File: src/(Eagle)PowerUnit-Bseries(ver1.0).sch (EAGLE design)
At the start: 51 parts

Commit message: XT60PWコネクタに変えた
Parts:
- removed IN+, IN-, OUT1+, OUT1-, OUT2+, OUT2-, OUT3+, OUT3-, THRU+, THRU-: PADS14, OKUDA_libraries:PADS14
- added CON1: XT90PW-M, amass:XT90PW-M
- added CON2: XT90PW-F, amass:XT90PW-F
- added CON3, CON4, CON5, CON6: XT60PW-F, amass:XT60PW-F
- added U1: LQFP64, STM32F446xC:LQFP64
- added U2: MCP2517FD, MCP2517FD:MCP2517FD
- H1, H2, H3, H4: value MOUNT-HOLE3.2 -> MOUNT-HOLE3.2(NORESIST); device holes:MOUNT-HOLE3.2 -> MOUNT-HOLE3.2(NORESIST):MOUNT-HOLE3.2(NORESIST)
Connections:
- net GND: now also CON1.-, CON2.-, H1.P$1, H2.P$1, H3.P$1, H4.P$1; no longer IN-.P$1, THRU-.P$1
- net N$1: now also CON3.-; no longer OUT1-.P$1
- net N$2: now also CON4.-; no longer OUT2-.P$1
- net N$4: now also CON3.+; no longer OUT1+.P$1
- net N$5: now also CON4.+; no longer OUT2+.P$1
- net N$6: no longer OUT3+.P$1
- net N$9: no longer OUT3-.P$1
- net VCC: now also CON1.+, CON2.+; no longer IN+.P$1, THRU+.P$1
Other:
- note removed: "e2011220_竹内一晴"
- note removed: "新電源基板(仮)_回路図"
- note removed: "部品選定完了☑"

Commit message: トランシーバ選定途中、XT60PW
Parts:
- removed EDGE5: 7-5530843-6, 7-5530843-6:7-5530843-6
- removed OUT4+, OUT4-: PADS14, OKUDA_libraries:PADS14
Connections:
- removed net NC: EDGE5.P7
- net DIR1: no longer EDGE5.P12
- net DIR2: no longer EDGE5.P11
- net DIR3: no longer EDGE5.P10
- net DIR4: no longer EDGE5.P9
- net GND2: no longer EDGE5.P8
- net LED: no longer EDGE5.P6
- net N$10: now also CON6.+; no longer OUT4+.P$1
- net N$13: now also CON6.-; no longer OUT4-.P$1
- net N$6: now also CON5.+
- net N$9: now also CON5.-
- net PWM1: no longer EDGE5.P1
- net PWM2: no longer EDGE5.P2
- net PWM3: no longer EDGE5.P3
- net PWM4: no longer EDGE5.P4
- net VCC2: no longer EDGE5.P5
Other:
- note removed: "MDC input"
- moved on the sheet: CON6, LED2, R1

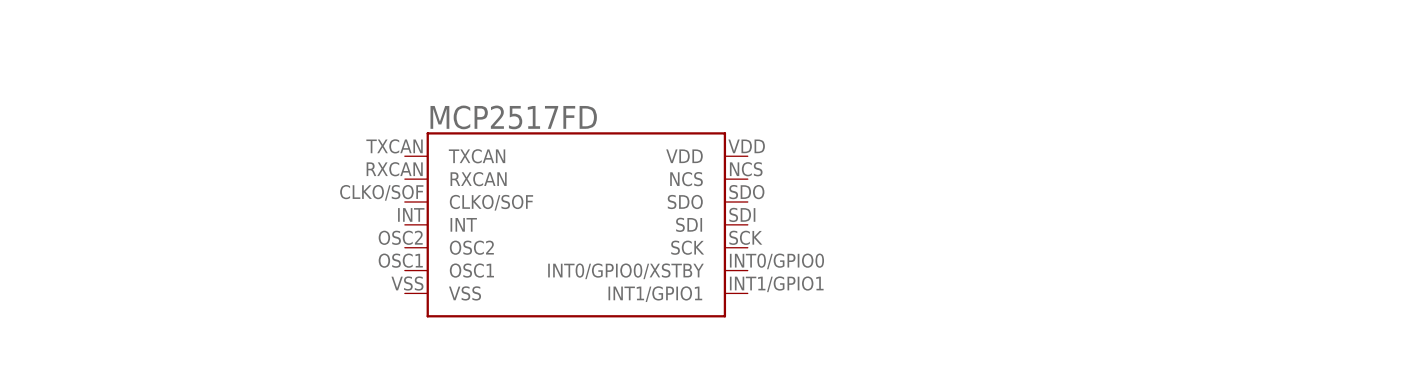
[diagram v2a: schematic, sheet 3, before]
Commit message: CANトランシーバの選定(クリスマスイブですよ？（笑）)
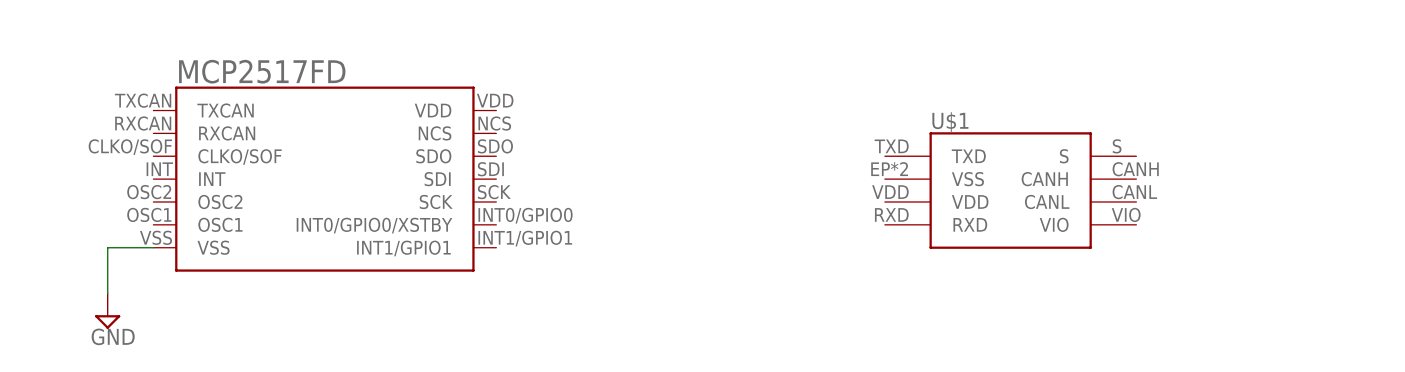
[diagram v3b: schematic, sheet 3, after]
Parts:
- added U$1: MCP2558FD, MCP2558FD:MCP2558FD
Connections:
- net GND: now also U2.VSS
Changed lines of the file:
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@@
 <part name="CON5" library="amass" deviceset="XT60" device="PW-F" package3d_urn="urn:adsk.eagle:package:38637521/2"/>
 <part name="CON6" library="amass" deviceset="XT60" device="PW-F" package3d_urn="urn:adsk.eagle:package:38637521/2"/>
+<part name="U$1" library="MCP2558FD" deviceset="MCP2558FD" device="" package3d_urn="urn:adsk.eagle:package:38673258/1"/>
+<part name="SUPPLY5" library="supply2" library_urn="urn:adsk.eagle:library:372" deviceset="GND" device=""/>
 </parts>
 <sheets>
@@
 <attribute name="SHEET" x="230.505" y="5.08" size="2.54" layer="94"/>
 </instance>
-<instance part="U2" gate="G$1" x="104.14" y="71.12" smashed="yes">
-<attribute name="VALUE" x="104.14" y="91.948" size="2.54" layer="96"/>
+<instance part="U2" gate="G$1" x="76.2" y="76.2" smashed="yes">
+<attribute name="VALUE" x="76.2" y="97.028" size="2.54" layer="96"/>
+</instance>
+<instance part="U$1" gate="G$1" x="160.02" y="78.74" smashed="yes">
+<attribute name="NAME" x="160.02" y="91.948" size="1.778" layer="95"/>
+</instance>
+<instance part="SUPPLY5" gate="GND" x="68.58" y="71.12" smashed="yes">
+<attribute name="VALUE" x="66.675" y="67.945" size="1.778" layer="96"/>
 </instance>
 </instances>
@@
 </busses>
 <nets>
+<net name="GND" class="0">
+<segment>
+<pinref part="U2" gate="G$1" pin="VSS"/>
+<pinref part="SUPPLY5" gate="GND" pin="GND"/>
+<wire x1="73.66" y1="78.74" x2="68.58" y2="78.74" width="0.1524" layer="91"/>
+<wire x1="68.58" y1="78.74" x2="68.58" y2="73.66" width="0.1524" layer="91"/>
+</segment>
+</net>
 </nets>
 </sheet>

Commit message: CAN周りの配線など
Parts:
- removed SV1: (no value), con-ml:ML10
- added JP2: (no value), pinhead:PINHD-1X2
- added R7: 120Ω, CR0603:CR0603
- added USB1: 5077CR-16SMC2-BK-TR, 5077CR-16SMC2-BK-TR:5077CR-16SMC2-BK-TR
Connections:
- new net +5V: USB1.VBUS
- new net CANH: R7.RIGHT, U$1.CANH
- new net CANL: JP2.2, U$1.CANL
- new net N$23: JP2.1, R7.LEFT
- new net N$27: U$1.TXD, U2.TXCAN
- new net N$28: U$1.RXD, U2.RXCAN
- net DIR1: no longer SV1.9
- net DIR2: no longer SV1.7
- net DIR3: no longer SV1.5
- net DIR4: no longer SV1.3
- net GND: now also U$1.VSS, USB1.GND, USB1.SHIELD
- net GND2: no longer SV1.1
- net PWM1: no longer SV1.10
- net PWM2: no longer SV1.8
- net PWM3: no longer SV1.6
- net PWM4: no longer SV1.4
- net VCC2: no longer SV1.2
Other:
- note removed: "logic input"
- moved on the sheet: C1, C2, CON1, CON2, CON3, CON4, CON5, CON6, CTRL1, CTRL2, EDGE1, EDGE2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

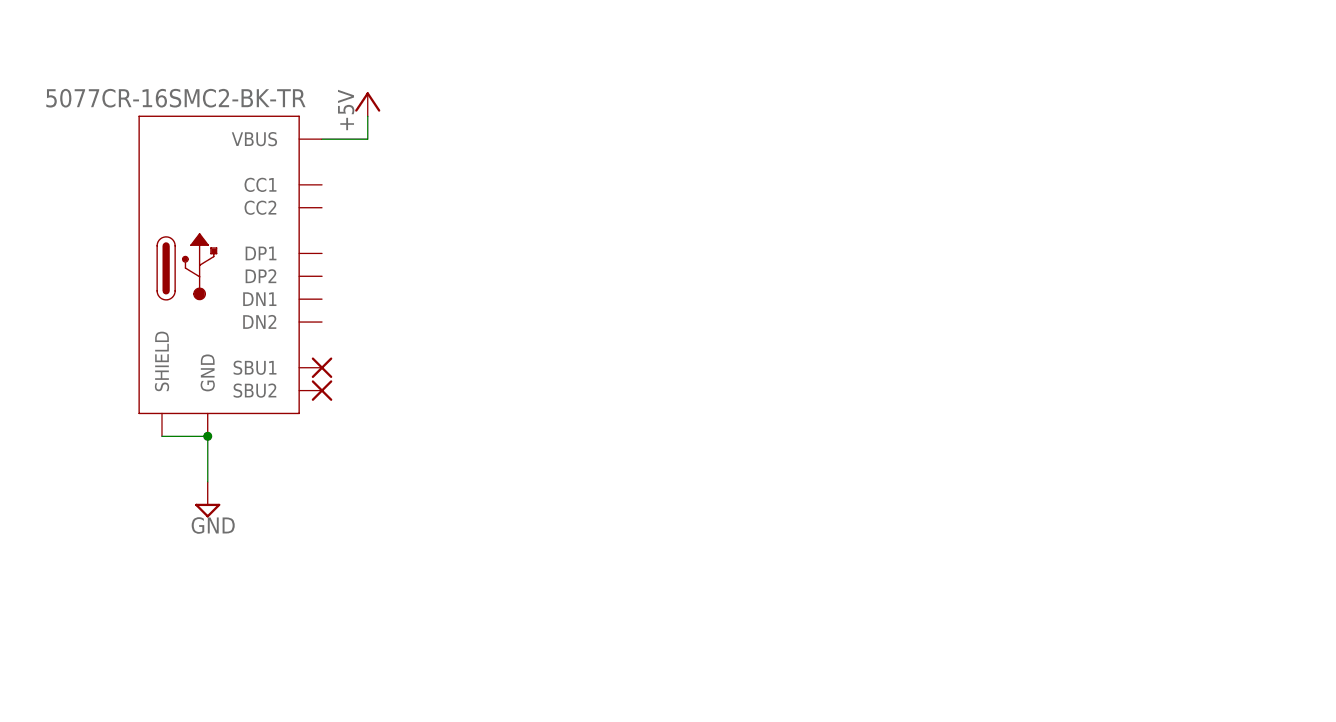
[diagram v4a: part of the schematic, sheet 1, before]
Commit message: レギュレータの追加など
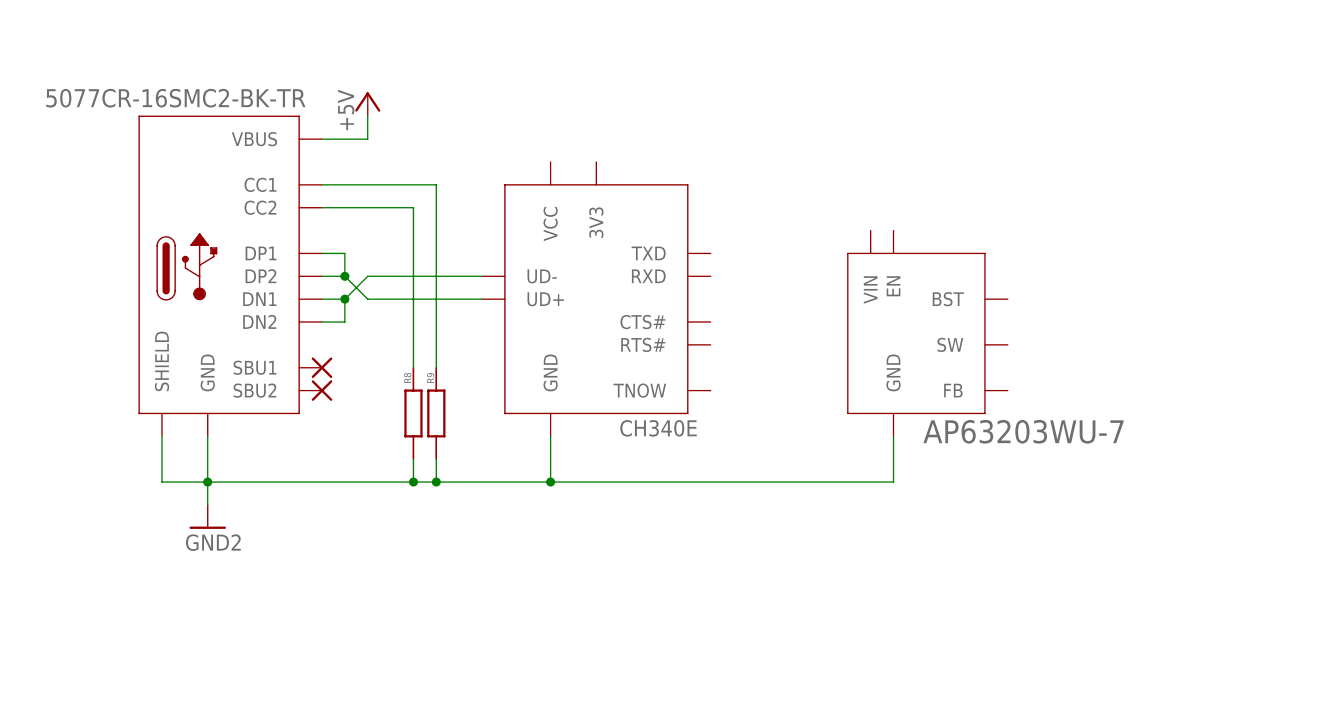
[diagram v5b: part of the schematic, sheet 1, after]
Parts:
- added R8, R9: (no value), CR0603:CR0603
- added U3: CH340E, CH340E:CH340E
- added U4: AP63203WU-7, AP63203WU-7:AP63203WU-7
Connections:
- new net N$29: R8.RIGHT, USB1.CC2
- new net N$30: R9.RIGHT, USB1.CC1
- new net N$31: U3.UD+, USB1.DP1, USB1.DP2
- new net N$32: U3.UD-, USB1.DN1, USB1.DN2
- net GND: no longer USB1.GND, USB1.SHIELD
- net GND2: now also R8.LEFT, R9.LEFT, U3.GND, U4.GND, USB1.GND, USB1.SHIELD
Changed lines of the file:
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@@
 <part name="USB1" library="5077CR-16SMC2-BK-TR" deviceset="5077CR-16SMC2-BK-TR" device=""/>
 <part name="FRAME4" library="frames" library_urn="urn:adsk.eagle:library:229" deviceset="FRAME_C_L" device=""/>
-<part name="SUPPLY7" library="supply2" library_urn="urn:adsk.eagle:library:372" deviceset="GND" device=""/>
 <part name="R7" library="CR0603" deviceset="CR0603" device="" value="120Ω"/>
 <part name="U$2" library="NC" deviceset="NC" device=""/>
 <part name="U$3" library="NC" deviceset="NC" device=""/>
 <part name="P+5" library="supply1" library_urn="urn:adsk.eagle:library:371" deviceset="+5V" device=""/>
+<part name="R8" library="CR0603" deviceset="CR0603" device=""/>
+<part name="R9" library="CR0603" deviceset="CR0603" device=""/>
+<part name="GND1" library="supply1" library_urn="urn:adsk.eagle:library:371" deviceset="GND" device=""/>
+<part name="U3" library="CH340E" deviceset="CH340E" device=""/>
+<part name="U4" library="AP63203WU-7" deviceset="AP63203WU-7" device=""/>
 </parts>
 <sheets>
@@
 <attribute name="DRAWING_NAME" x="469.9" y="19.05" size="2.54" layer="94"/>
 </instance>
-<instance part="SUPPLY7" gate="GND" x="106.68" y="88.9" smashed="yes">
-<attribute name="VALUE" x="104.775" y="85.725" size="1.778" layer="96"/>
-</instance>
 <instance part="U$2" gate="G$1" x="119.38" y="101.6" smashed="yes"/>
 <instance part="U$3" gate="G$1" x="119.38" y="104.14" smashed="yes"/>
 <instance part="P+5" gate="1" x="124.46" y="134.62" smashed="yes">
 <attribute name="VALUE" x="122.936" y="130.302" size="1.778" layer="96" rot="R90"/>
+</instance>
+<instance part="R8" gate="G$1" x="129.54" y="99.06" smashed="yes" rot="R90">
+<attribute name="NAME" x="129.286" y="102.362" size="0.762" layer="95" rot="R90"/>
+<attribute name="VALUE" x="130.556" y="102.362" size="0.762" layer="96" rot="R90"/>
+</instance>
+<instance part="R9" gate="G$1" x="132.08" y="99.06" smashed="yes" rot="R90">
+<attribute name="NAME" x="131.826" y="102.362" size="0.762" layer="95" rot="R90"/>
+<attribute name="VALUE" x="133.096" y="102.362" size="0.762" layer="96" rot="R90"/>
+</instance>
+<instance part="GND1" gate="1" x="106.68" y="86.36" smashed="yes"/>
+<instance part="U3" gate="G$1" x="139.7" y="99.06" smashed="yes">
+<attribute name="VALUE" x="152.4" y="96.52" size="1.778" layer="96"/>
+</instance>
+<instance part="U4" gate="G$1" x="177.8" y="99.06" smashed="yes">
+<attribute name="VALUE" x="186.182" y="95.758" size="2.54" layer="96"/>
 </instance>
 </instances>
@@
 <wire x1="27.94" y1="17.78" x2="17.78" y2="17.78" width="0.1524" layer="91"/>
 <junction x="17.78" y="17.78"/>
-</segment>
-<segment>
-<pinref part="USB1" gate="G$1" pin="SHIELD"/>
-<pinref part="USB1" gate="G$1" pin="GND"/>
-<wire x1="101.6" y1="96.52" x2="106.68" y2="96.52" width="0.1524" layer="91"/>
-<pinref part="SUPPLY7" gate="GND" pin="GND"/>
-<wire x1="106.68" y1="96.52" x2="106.68" y2="91.44" width="0.1524" layer="91"/>
-<junction x="106.68" y="96.52"/>
 </segment>
 </net>
@@
 <wire x1="381" y1="287.02" x2="370.84" y2="287.02" width="0.1524" layer="91"/>
 <label x="368.3" y="287.02" size="1.778" layer="95"/>
+</segment>
+<segment>
+<pinref part="USB1" gate="G$1" pin="SHIELD"/>
+<wire x1="101.6" y1="96.52" x2="101.6" y2="91.44" width="0.1524" layer="91"/>
+<wire x1="101.6" y1="91.44" x2="106.68" y2="91.44" width="0.1524" layer="91"/>
+<pinref part="GND1" gate="1" pin="GND"/>
+<wire x1="106.68" y1="91.44" x2="106.68" y2="88.9" width="0.1524" layer="91"/>
+<pinref part="USB1" gate="G$1" pin="GND"/>
+<wire x1="106.68" y1="91.44" x2="106.68" y2="96.52" width="0.1524" layer="91"/>
+<junction x="106.68" y="91.44"/>
+<wire x1="106.68" y1="91.44" x2="129.54" y2="91.44" width="0.1524" layer="91"/>
+<pinref part="U3" gate="G$1" pin="GND"/>
+<wire x1="129.54" y1="91.44" x2="132.08" y2="91.44" width="0.1524" layer="91"/>
+<wire x1="132.08" y1="91.44" x2="144.78" y2="91.44" width="0.1524" layer="91"/>
+<wire x1="144.78" y1="91.44" x2="144.78" y2="96.52" width="0.1524" layer="91"/>
+<pinref part="R9" gate="G$1" pin="LEFT"/>
+<wire x1="132.08" y1="93.98" x2="132.08" y2="91.44" width="0.1524" layer="91"/>
+<junction x="132.08" y="91.44"/>
+<pinref part="R8" gate="G$1" pin="LEFT"/>
+<wire x1="129.54" y1="93.98" x2="129.54" y2="91.44" width="0.1524" layer="91"/>
+<junction x="129.54" y="91.44"/>
+<label x="104.14" y="83.82" size="1.778" layer="95"/>
+<pinref part="U4" gate="G$1" pin="GND"/>
+<wire x1="144.78" y1="91.44" x2="182.88" y2="91.44" width="0.1524" layer="91"/>
+<wire x1="182.88" y1="91.44" x2="182.88" y2="96.52" width="0.1524" layer="91"/>
+<junction x="144.78" y="91.44"/>
 </segment>
 </net>
@@
 </segment>
 </net>
+<net name="N$29" class="0">
+<segment>
+<pinref part="USB1" gate="G$1" pin="CC2"/>
+<pinref part="R8" gate="G$1" pin="RIGHT"/>
+<wire x1="119.38" y1="121.92" x2="129.54" y2="121.92" width="0.1524" layer="91"/>
+<wire x1="129.54" y1="121.92" x2="129.54" y2="104.14" width="0.1524" layer="91"/>
+</segment>
+</net>
+<net name="N$30" class="0">
+<segment>
+<pinref part="USB1" gate="G$1" pin="CC1"/>
+<pinref part="R9" gate="G$1" pin="RIGHT"/>
+<wire x1="119.38" y1="124.46" x2="132.08" y2="124.46" width="0.1524" layer="91"/>
+<wire x1="132.08" y1="124.46" x2="132.08" y2="104.14" width="0.1524" layer="91"/>
+</segment>
+</net>
+<net name="N$31" class="0">
+<segment>
+<pinref part="USB1" gate="G$1" pin="DP1"/>
+<wire x1="119.38" y1="116.84" x2="121.92" y2="116.84" width="0.1524" layer="91"/>
+<wire x1="121.92" y1="116.84" x2="121.92" y2="114.3" width="0.1524" layer="91"/>
+<pinref part="USB1" gate="G$1" pin="DP2"/>
+<wire x1="121.92" y1="114.3" x2="119.38" y2="114.3" width="0.1524" layer="91"/>
+<wire x1="121.92" y1="114.3" x2="124.46" y2="111.76" width="0.1524" layer="91"/>
+<junction x="121.92" y="114.3"/>
+<pinref part="U3" gate="G$1" pin="UD+"/>
+<wire x1="124.46" y1="111.76" x2="137.16" y2="111.76" width="0.1524" layer="91"/>
+</segment>
+</net>
+<net name="N$32" class="0">
+<segment>
+<pinref part="USB1" gate="G$1" pin="DN1"/>
+<wire x1="119.38" y1="111.76" x2="121.92" y2="111.76" width="0.1524" layer="91"/>
+<wire x1="121.92" y1="111.76" x2="121.92" y2="109.22" width="0.1524" layer="91"/>
+<pinref part="USB1" gate="G$1" pin="DN2"/>
+<wire x1="121.92" y1="109.22" x2="119.38" y2="109.22" width="0.1524" layer="91"/>
+<wire x1="121.92" y1="111.76" x2="124.46" y2="114.3" width="0.1524" layer="91"/>
+<junction x="121.92" y="111.76"/>
+<pinref part="U3" gate="G$1" pin="UD-"/>
+<wire x1="124.46" y1="114.3" x2="137.16" y2="114.3" width="0.1524" layer="91"/>
+</segment>
+</net>
